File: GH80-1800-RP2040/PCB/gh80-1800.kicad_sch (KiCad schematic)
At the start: 278 parts, among them J1 USB_mini_micro_B, J2 ISP, J3 USB Header, J4 USB_mini_micro_B, J5 USB_mini_micro_B, K1 KEYSW, K10 KEYSW, K100 KEYSW, K101 KEYSW, K102 KEYSW, K103 KEYSW, K104 KEYSW, K105 KEYSW, K107 KEYSW, K108 KEYSW, K109 KEYSW, K11 KEYSW, K110 KEYSW, K12 KEYSW, K13 KEYSW, K14 KEYSW, K15 KEYSW, K16 KEYSW, K17 KEYSW, K18 KEYSW, K18-1 KEYSW, K19 KEYSW, K2 KEYSW, K20 KEYSW, K21 KEYSW, K22 KEYSW, K23 KEYSW, K24 KEYSW, K25 KEYSW, K26 KEYSW, K27 KEYSW, K28 KEYSW, K29 KEYSW, K3 KEYSW, K30 KEYSW, K31 KEYSW, K32 KEYSW, K33 KEYSW, K34 KEYSW, K35 KEYSW, K36 KEYSW, K37 KEYSW, K38 KEYSW, K39 KEYSW, K4 KEYSW, K40 KEYSW, K41 KEYSW, K42 KEYSW, K43 KEYSW, K44 KEYSW, K45 KEYSW, K46 KEYSW, K47 KEYSW, K48 KEYSW, K49 KEYSW, K5 KEYSW, K50 KEYSW, K51 KEYSW, K52 KEYSW, K53 KEYSW, K54 KEYSW, K55 KEYSW, K55-1 KEYSW, K56 KEYSW, K57 KEYSW, K58 KEYSW, K59 KEYSW, K6 KEYSW, K60 KEYSW, K61 KEYSW, K62 KEYSW, K63 KEYSW, K64 KEYSW, K65 KEYSW, K66 KEYSW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

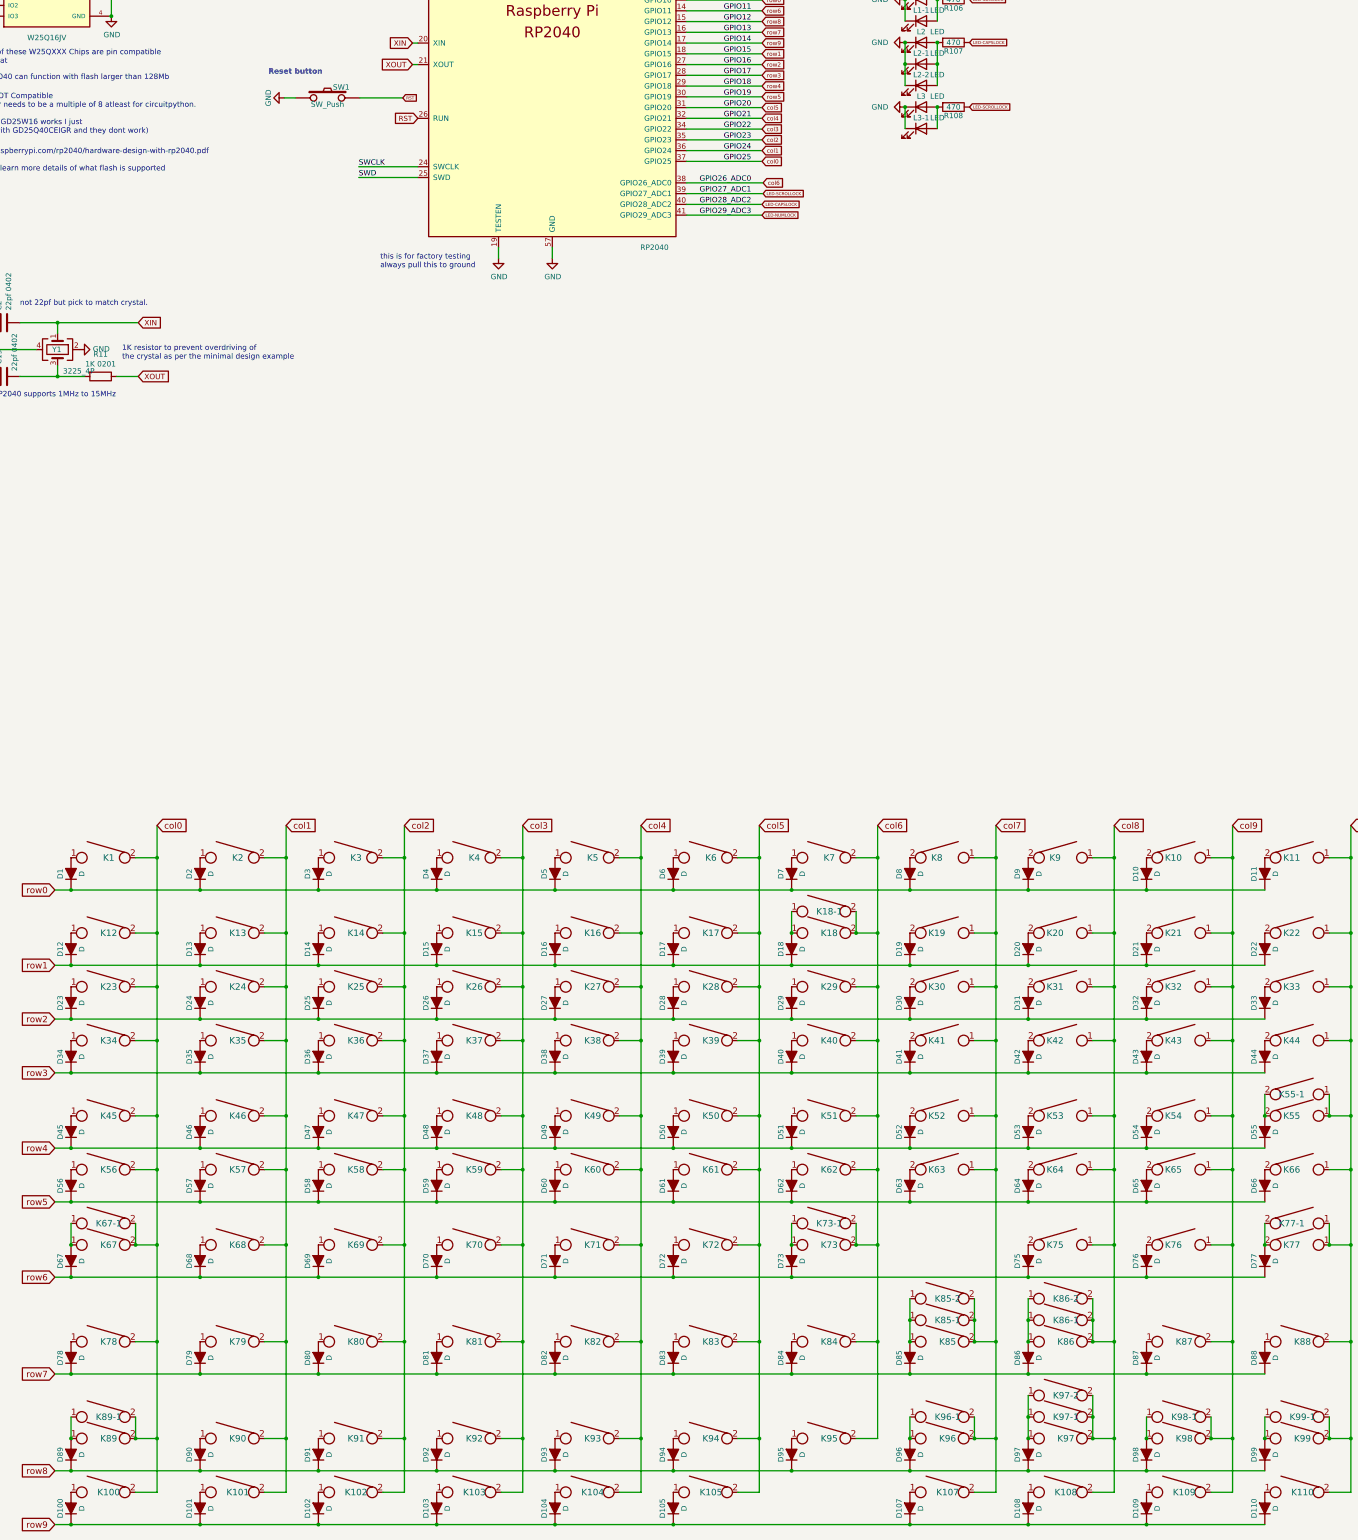
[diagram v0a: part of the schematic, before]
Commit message: Added debug pads and reset button, Generated updated Gerber, BOM and CPL
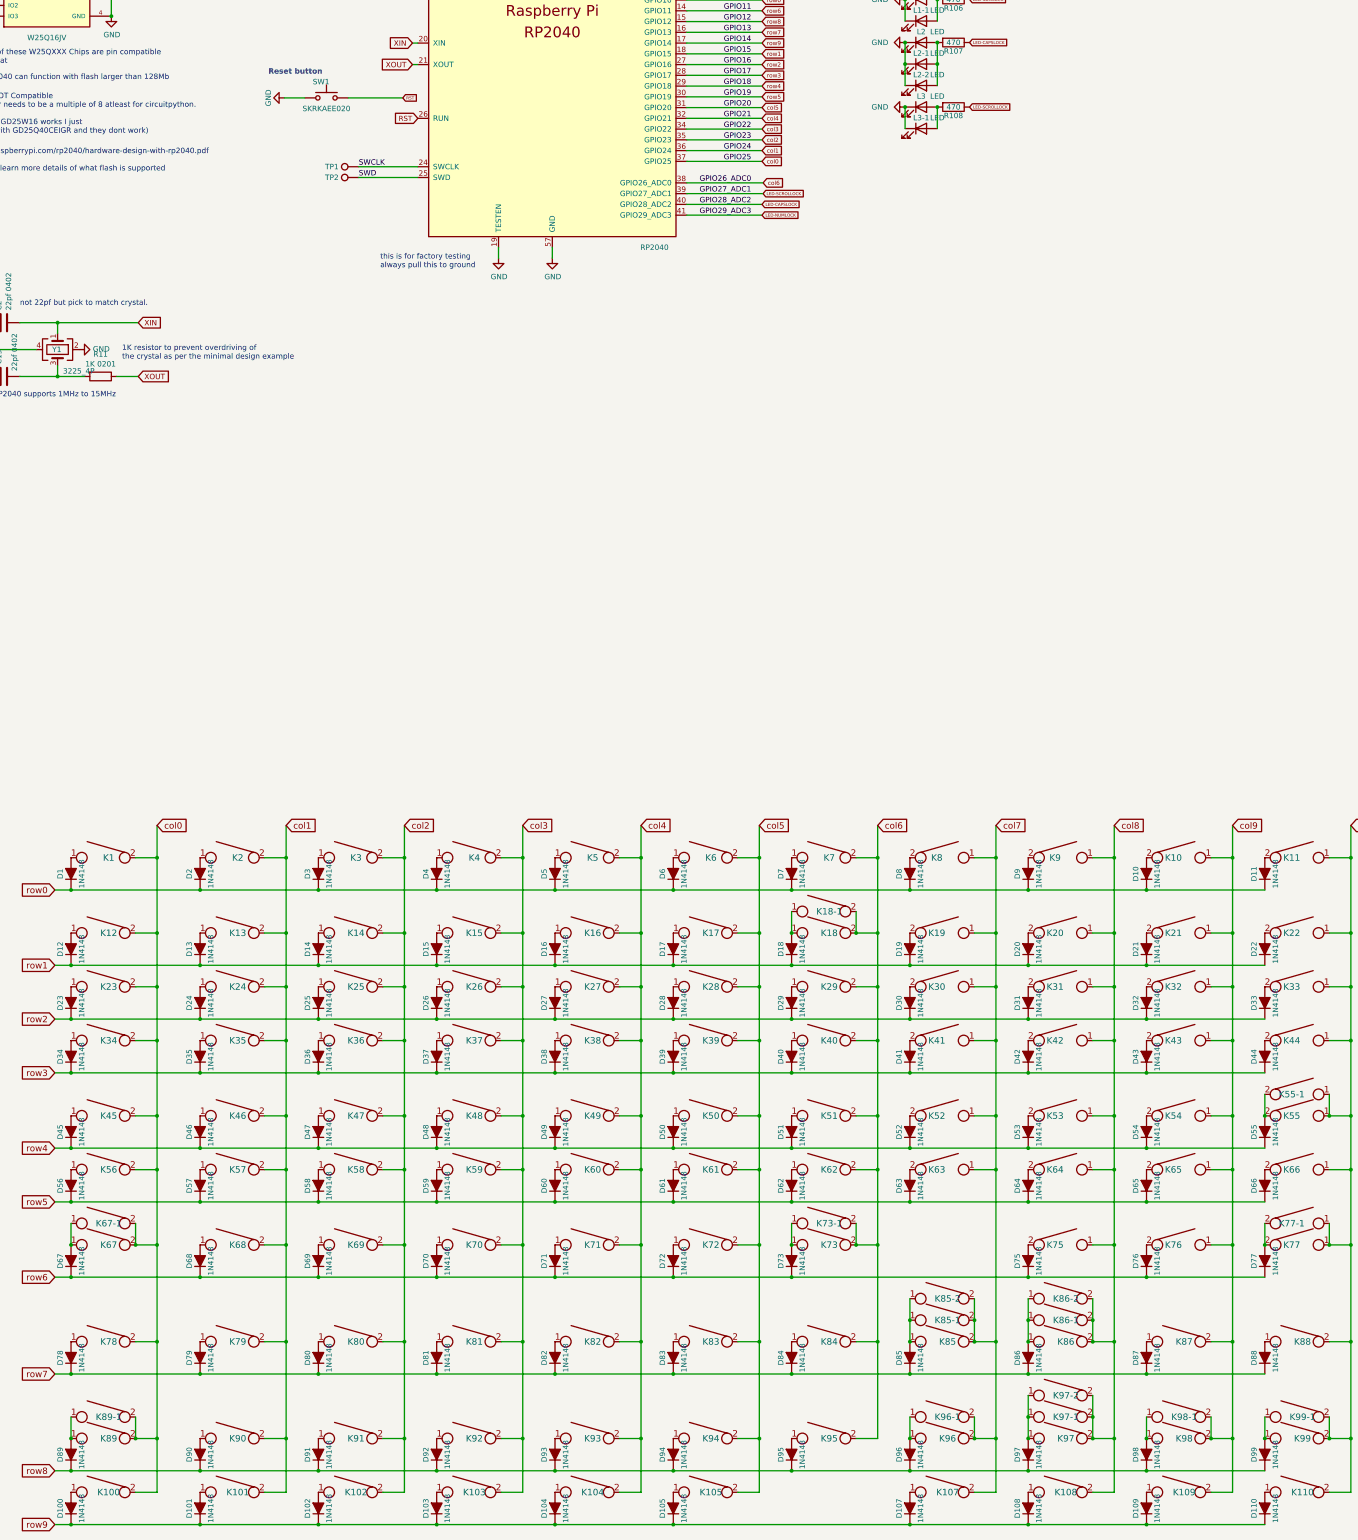
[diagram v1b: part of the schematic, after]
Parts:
- removed SW1: SW_Push, Buttons_Switches_SMD:SW_SPST_TL3342, symbol keyboard_parts:SW_PUSH
- added SW1: SKRKAEE020, Button_Switch_SMD:SW_Push_SPST_NO_Alps_SKRK, symbol Switch:SW_Push
- added TP1, TP2: TestPoint, TestPoint:TestPoint_Pad_D1.0mm, symbol Connector:TestPoint
- D1, D10, D100, D101, D102, D103, D104, D105, D107, D108, D109, D11, D110, D12, D13, D14, D15, D16, D17, D18, D19, D2, D20, D21, D22, D23, D24, D25, D26, D27, D28, D29, D3, D30, D31, D32, D33, D34, D35, D36, D37, D38, D39, D4, D40, D41, D42, D43, D44, D45, D46, D47, D48, D49, D5, D50, D51, D52, D53, D54, D55, D56, D57, D58, D59, D6, D60, D61, D62, D63, D64, D65, D66, D67, D68, D69, D7, D70, D71, D72, D73, D75, D76, D77, D78, D79, D8, D80, D81, D82, D83, D84, D85, D86, D87, D88, D89, D9, D90, D91, D92, D93, D94, D95, D96, D97, D98, D99: value D -> 1N4148
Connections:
- net GND: now also SW1.2
- net RST: now also SW1.1
- net SWCLK: now also TP1.1
- net SWD: now also TP2.1
